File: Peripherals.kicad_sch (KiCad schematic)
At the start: 15 parts, among them J3 1040310811, U5 LSM6DSV

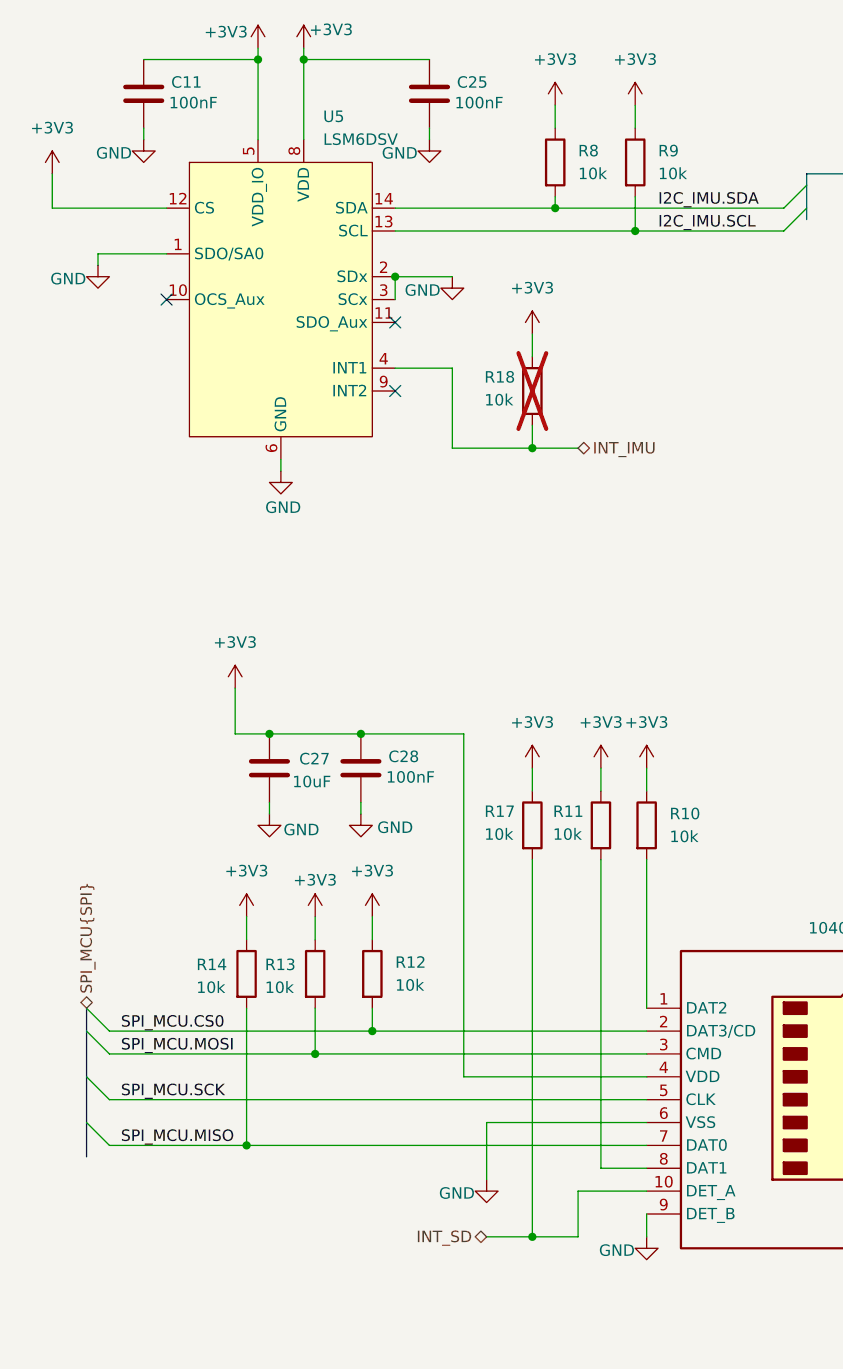
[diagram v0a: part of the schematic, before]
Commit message: added schematics comments of review 1
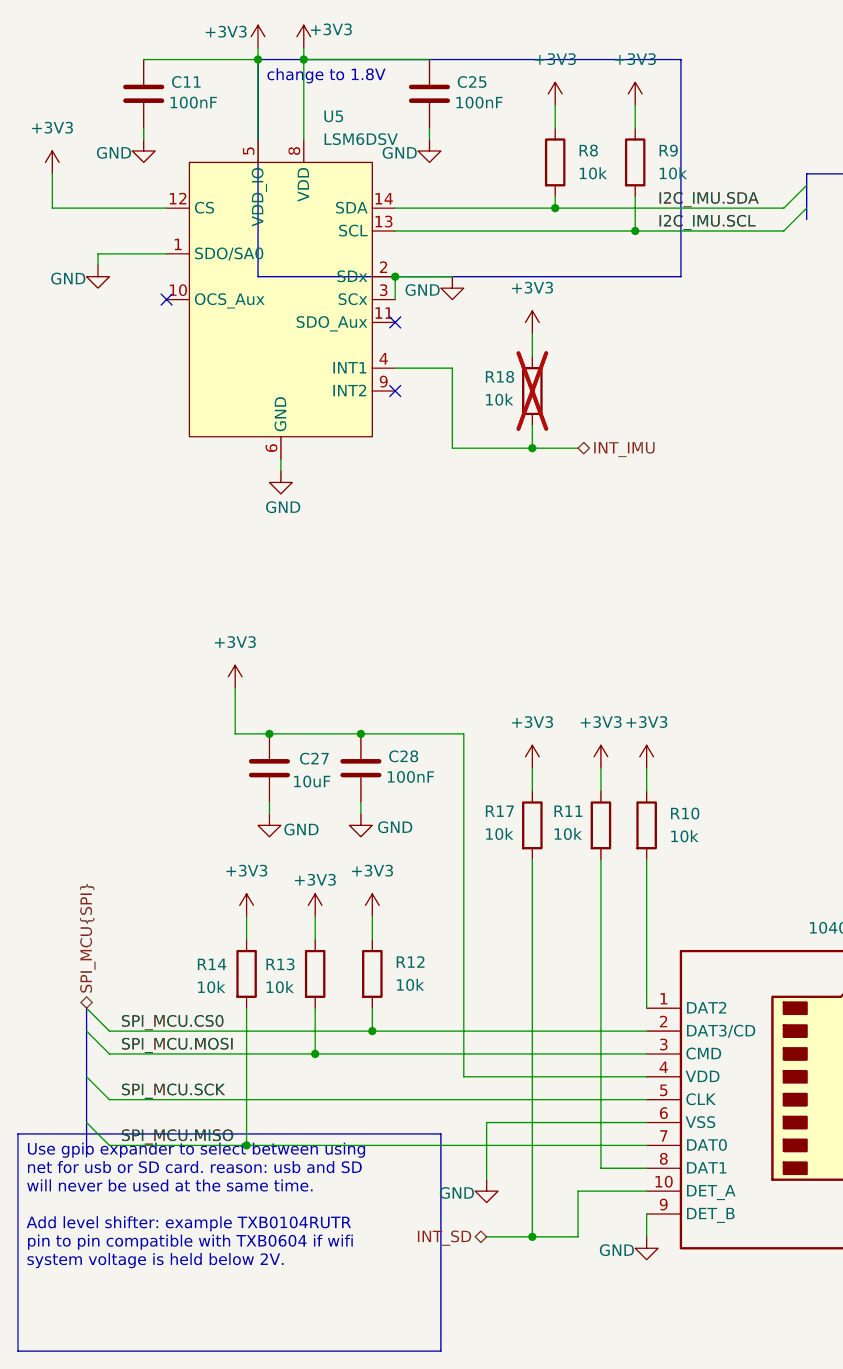
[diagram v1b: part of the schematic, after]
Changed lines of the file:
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@@
 	(generator_version "10.0")
 	(paper "A4")
+	(text_box "change to 1.8V"
+		(exclude_from_sim no)
+		(at 53.34 41.91 0)
+		(size 46.99 24.13)
+		(margins 0.9525 0.9525 0.9525 0.9525)
+		(stroke
+			(width 0)
+			(type solid)
+		)
+		(fill
+			(type color)
+			(color 255 153 0 1)
+		)
+		(effects
+			(font
+				(size 1.27 1.27)
+			)
+			(justify left top)
+		)
+	)
+	(text_box "Use gpio expander to select between using net for usb or SD card. reason: usb and SD will never be used at the same time. \n\nAdd level shifter: example TXB0104RUTR \npin to pin compatible with TXB0604 if wifi system voltage is held below 2V."
+		(exclude_from_sim no)
+		(at 26.67 161.29 0)
+		(size 46.99 24.13)
+		(margins 0.9525 0.9525 0.9525 0.9525)
+		(stroke
+			(width 0)
+			(type solid)
+		)
+		(fill
+			(type color)
+			(color 255 153 0 1)
+		)
+		(effects
+			(font
+				(size 1.27 1.27)
+			)
+			(justify left top)
+		)
+	)
 	(junction
 		(at 52.07 162.56)

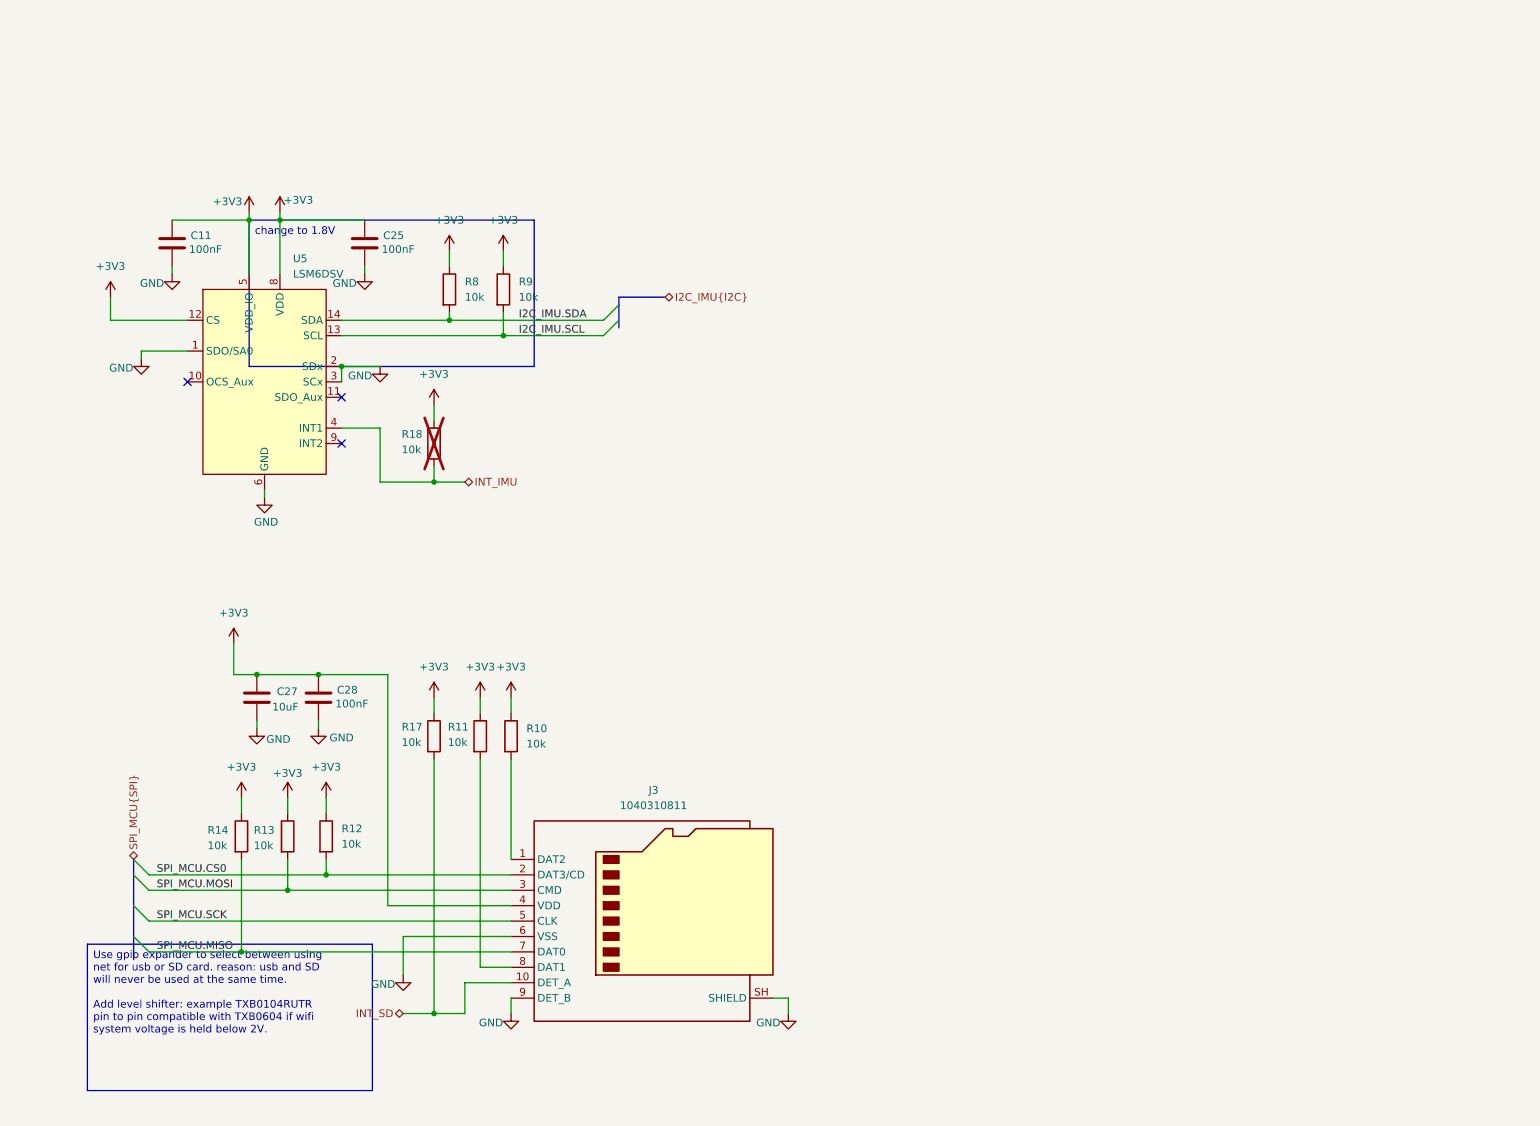
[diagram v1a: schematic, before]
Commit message: changes after first review: add lvl shifters, board at 1v8, new power tree
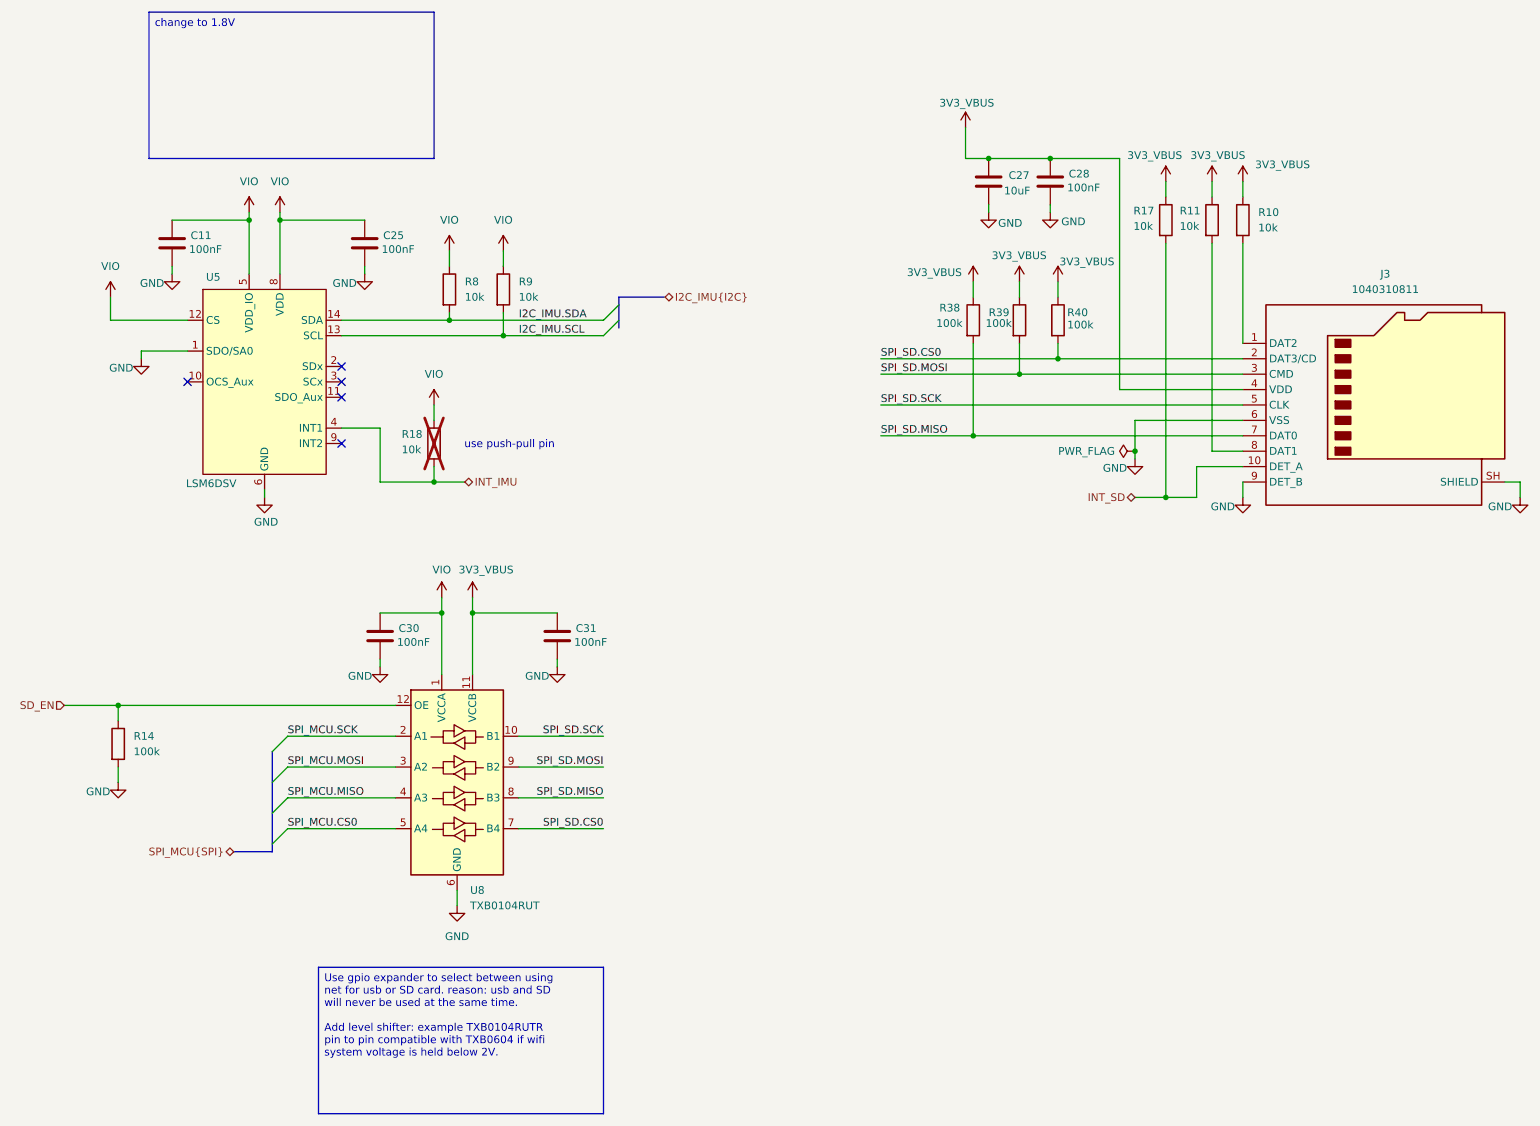
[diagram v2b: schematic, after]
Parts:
- removed R12, R13, R14: 10k, Resistor_SMD:R_0402_1005Metric, symbol #dzdb:g_res/R-10k-0402
- added C30, C31: 100nF, Capacitor_SMD:C_0603_1608Metric, symbol #dzdb:g_cap/C-100n-0603
- added R14, R38, R39, R40: 100k, Resistor_SMD:R_0402_1005Metric, symbol #dzdb:g_res/R-100k-0402
- added U8: TXB0104RUT, Package_DFN_QFN:Texas_R-PUQFN-N12, symbol Logic_LevelTranslator:TXB0104RUT
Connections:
- net GND: now also C30.2, C31.2, R14.2, U8.6 (GND); no longer U5.2 (SDx), U5.3 (SCx)
- net SPI_MCU.CS0: now also U8.5 (A4); no longer J3.2 (DAT3/CD)
- net SPI_MCU.MISO: now also U8.4 (A3); no longer J3.7 (DAT0)
- net SPI_MCU.MOSI: now also U8.3 (A2); no longer J3.3 (CMD)
- net SPI_MCU.SCK: now also U8.2 (A1); no longer J3.5 (CLK)
- net +3V3 renamed VIO
- net VIO: now also C30.1, U8.1 (VCCA); no longer C27.1, C28.1, J3.4 (VDD), R10.1, R11.1, R17.1
- new net 3V3_VBUS: C27.1, C28.1, C31.1, J3.4 (VDD), R10.1, R11.1, R17.1, R38.1, R39.1, R40.1, U8.11 (VCCB)
- new net SD_EN: R14.1, U8.12 (OE)
- new net SPI_SD.CS0: J3.2 (DAT3/CD), R40.2, U8.7 (B4)
- new net SPI_SD.MISO: J3.7 (DAT0), R38.2, U8.8 (B3)
- new net SPI_SD.MOSI: J3.3 (CMD), R39.2, U8.9 (B2)
- new net SPI_SD.SCK: J3.5 (CLK), U8.10 (B1)
- no-connect marks 3 -> 5
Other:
- note added: "use push-pull pin"
- moved on the sheet: C27, C28, J3, R10, R11, R17

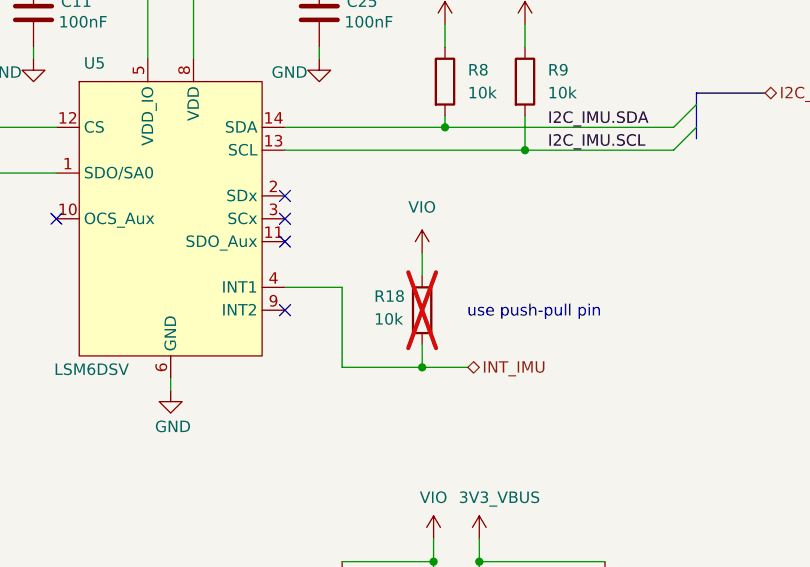
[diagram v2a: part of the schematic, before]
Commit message: updated schematic and initial pcb placement
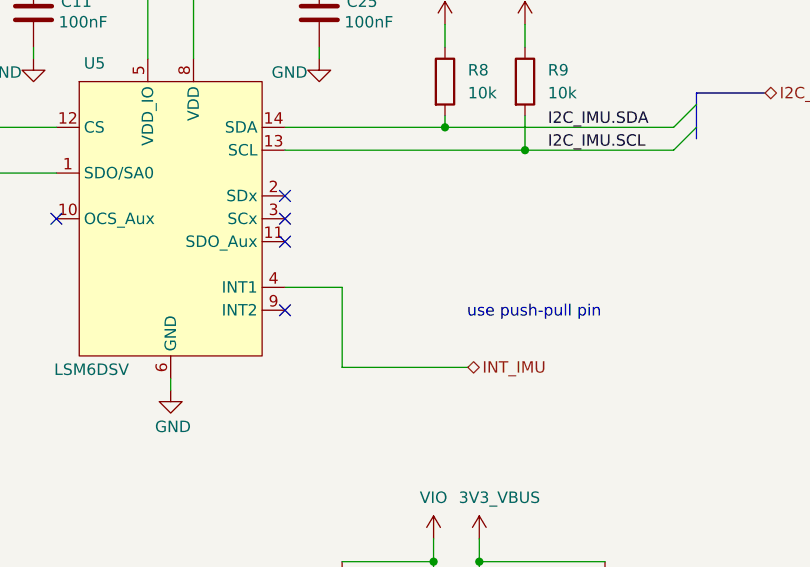
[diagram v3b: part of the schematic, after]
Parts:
- removed R18: 10k, Resistor_SMD:R_0402_1005Metric, symbol #dzdb:g_res/R-10k-0402
